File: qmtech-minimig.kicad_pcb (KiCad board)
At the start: 4 copper layers, 142.2 x 92 mm, 120 parts, among them IC1 RTL8211EG-VB-CG, J1 DB9_Male, J2 DB9_Male, J3 SCHA5B0200, J4 ARM_JTAG, J5 AUDIO-CONNECTOR-6P-SMD-344003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, J6 Mini-DIN-6, J7 HDMI_D_1.4, J8 HR911130A, SW1 SW_Push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

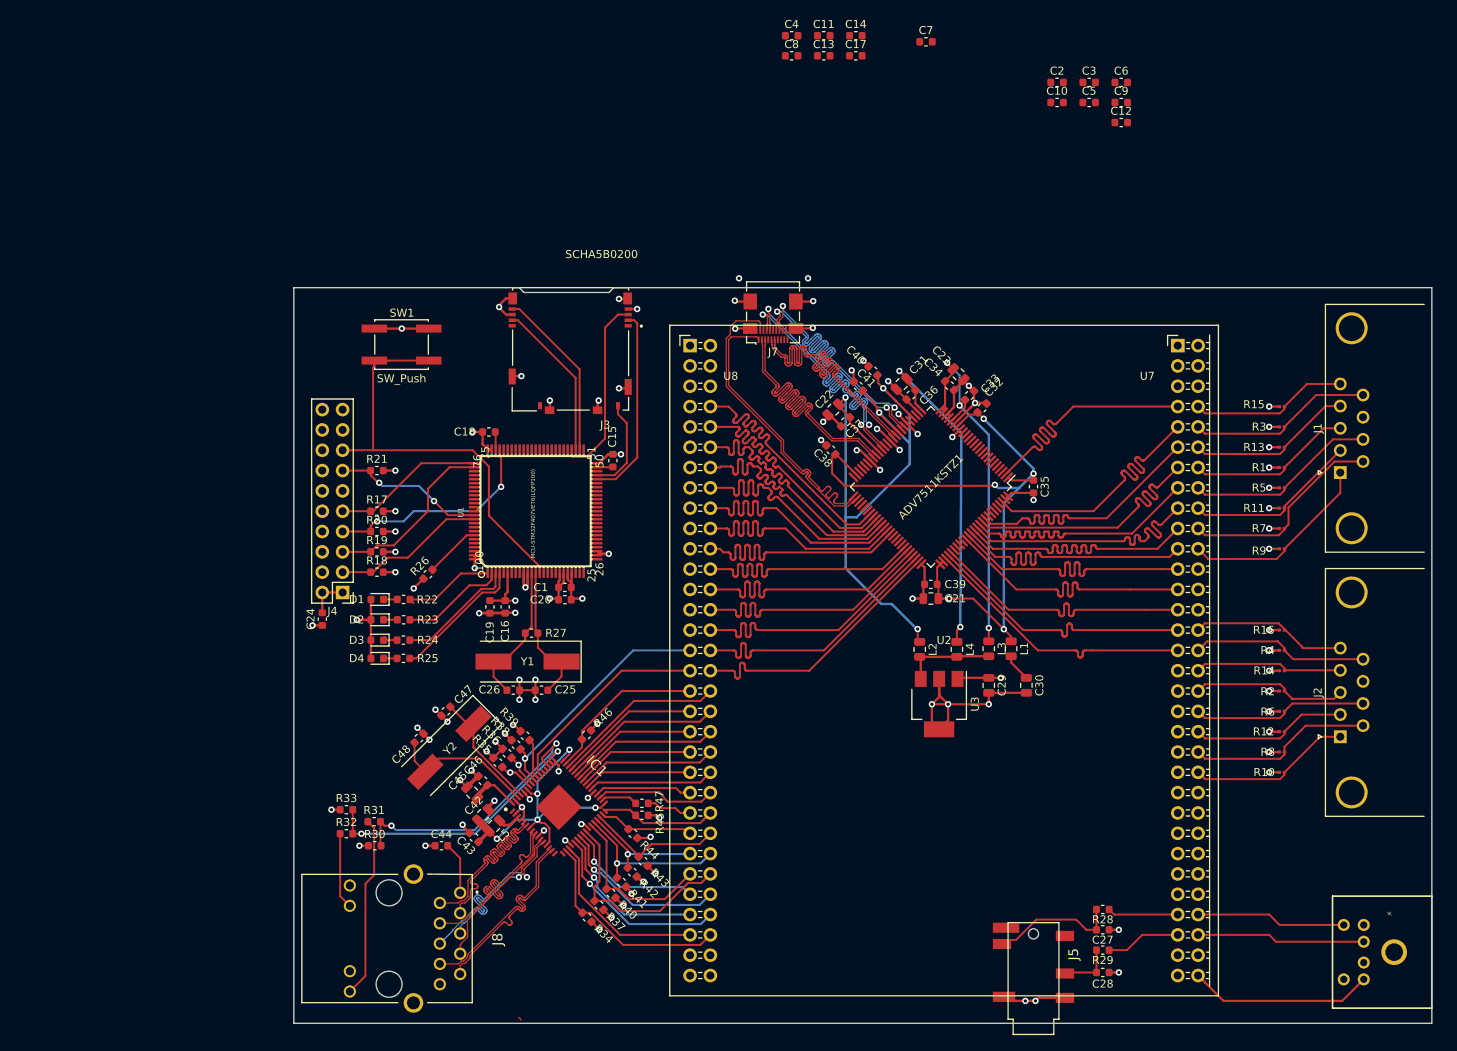
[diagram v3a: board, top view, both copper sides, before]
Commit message: Added protection diodes to the joystick ports.
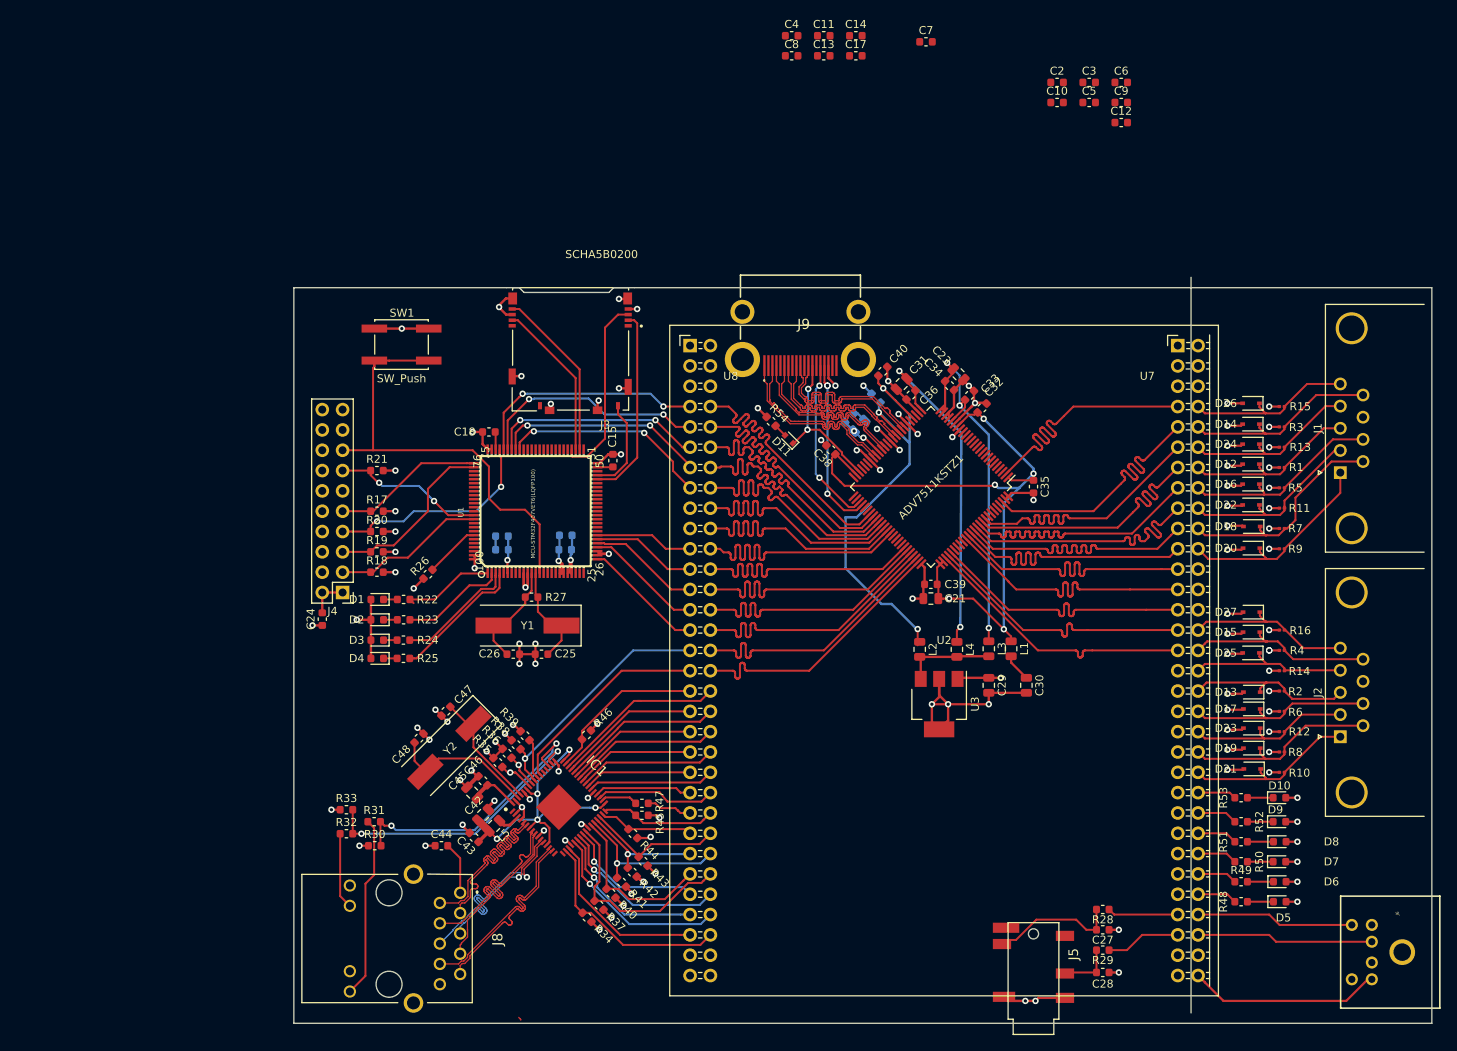
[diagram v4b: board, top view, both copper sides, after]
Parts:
- removed J7: HDMI_D_1.4, Connector_HDMI:HDMI_Micro-D_Molex_46765-0x01
- added D10: LED0, LED_SMD:LED_0603_1608Metric, F.Cu at (174.0, 127.0)
- added D11: D, Diode_SMD:D_SOD-523, F.Cu at (112.7, 82.2)
- added D12: D_Zener 3.6V BZT52C395, Diode_SMD:D_SOD-323, F.Cu at (170.4, 85.3)
- added D13: D_Zener 3.6V BZT52C395, Diode_SMD:D_SOD-323, F.Cu at (170.6, 113.8)
- added D14: D_Zener 3.6V BZT52C395, Diode_SMD:D_SOD-323, F.Cu at (170.4, 80.3)
- added D15: D_Zener 3.6V BZT52C395, Diode_SMD:D_SOD-323, F.Cu at (170.5, 106.3)
- added D16: D_Zener 3.6V BZT52C395, Diode_SMD:D_SOD-323, F.Cu at (170.4, 87.8)
- added D17: D_Zener 3.6V BZT52C395, Diode_SMD:D_SOD-323, F.Cu at (170.6, 115.9)
- added D18: D_Zener 3.6V BZT52C395, Diode_SMD:D_SOD-323, F.Cu at (170.6, 93.1)
- added D19: D_Zener 3.6V BZT52C395, Diode_SMD:D_SOD-323, F.Cu at (170.6, 120.8)
- added D20: D_Zener 3.6V BZT52C395, Diode_SMD:D_SOD-323, F.Cu at (170.5, 95.8)
- added D21: D_Zener 3.6V BZT52C395, Diode_SMD:D_SOD-323, F.Cu at (170.6, 123.4)
- added D22: D_Zener 3.6V BZT52C395, Diode_SMD:D_SOD-323, F.Cu at (170.4, 90.4)
- added D23: D_Zener 3.6V BZT52C395, Diode_SMD:D_SOD-323, F.Cu at (170.6, 118.3)
- added D24: D_Zener 3.6V BZT52C395, Diode_SMD:D_SOD-323, F.Cu at (170.4, 82.8)
- added D25: D_Zener 3.6V BZT52C395, Diode_SMD:D_SOD-323, F.Cu at (170.4, 108.9)
- added D26: D_Zener 3.6V BZT52C395, Diode_SMD:D_SOD-323, F.Cu at (170.4, 77.7)
- added D27: D_Zener 3.6V BZT52C395, Diode_SMD:D_SOD-323, F.Cu at (170.5, 103.8)
- added D5: LED5, LED_SMD:LED_0603_1608Metric, F.Cu at (174.0, 140.0)
- added D6: LED4, LED_SMD:LED_0603_1608Metric, F.Cu at (174.0, 137.5)
- added D7: LED3, LED_SMD:LED_0603_1608Metric, F.Cu at (174.0, 135.0)
- added D8: LED2, LED_SMD:LED_0603_1608Metric, F.Cu at (174.0, 132.5)
- added D9: LED1, LED_SMD:LED_0603_1608Metric, F.Cu at (174.0, 130.0)
- added J9: 47151-0001, 47151-0001-HDMI:47151-0001, F.Cu at (114.1, 61.7)
- added R48: 1k, Resistor_SMD:R_0603_1608Metric, F.Cu at (169.2, 140.0)
- added R49: 1k, Resistor_SMD:R_0603_1608Metric, F.Cu at (169.2, 137.5)
- added R50: 1k, Resistor_SMD:R_0603_1608Metric, F.Cu at (169.2, 135.0)
- added R51: 1k, Resistor_SMD:R_0603_1608Metric, F.Cu at (169.2, 132.5)
- added R52: 1k, Resistor_SMD:R_0603_1608Metric, F.Cu at (169.2, 130.0)
- added R53: 1k, Resistor_SMD:R_0603_1608Metric, F.Cu at (169.2, 127.0)
- added R54: 27K, Resistor_SMD:R_0603_1608Metric, F.Cu at (110.5, 80.0)
- C1, C16, C19, C20, C22, C37, C41: moved to B.Cu
- moved C16 8.86 mm to (76.8, 94.3), turned to 0 degrees
- moved C20 8.05 mm to (84.8, 94.2)
- moved C19 7.31 mm to (76.8, 96.0), turned to 180 degrees
- moved C1 4.71 mm to (84.7, 96.0)
- moved C25 4.50 mm to (81.8, 109.1)
- moved C26 4.50 mm to (78.2, 109.1)
- moved R27 4.50 mm to (80.5, 101.9)
- moved Y1 4.50 mm to (80.0, 105.5)
- moved C22 3.83 mm to (121.5, 80.5), turned to 45 degrees
- moved C41 2.67 mm to (123.6, 77.1)
- moved C40 1.23 mm to (124.4, 73.7), turned to 225 degrees
- moved J6 1.01 mm to (194.1, 146.3)
- moved C37 0.71 mm to (120.3, 79.5), turned to 45 degrees
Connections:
- net Net-(ADV7511KSTZ1-Pad12) renamed ADV_I2S0
- net Net-(ADV7511KSTZ1-Pad13) renamed ADV_I2S1
- net Net-(ADV7511KSTZ1-Pad14) renamed ADV_I2S2
- net Net-(ADV7511KSTZ1-Pad15) renamed ADV_I2S3
- net Net-(ADV7511KSTZ1-Pad16) renamed ADV_SCLK
- net Net-(ADV7511KSTZ1-Pad17) renamed ADV_LRCLK
- net Net-(ADV7511KSTZ1-Pad50) renamed ADV_CEC_CLK
- net Net-(ADV7511KSTZ1-Pad55) renamed ADV_SCL
- net Net-(ADV7511KSTZ1-Pad56) renamed ADV_SDA
- ADV7511KSTZ1 pad 48: Net-(ADV7511KSTZ1-Pad48) -> ADV_CEC
- ADV7511KSTZ1 pad 53: Net-(ADV7511KSTZ1-Pad53) -> ADV_DDCSCL
- ADV7511KSTZ1 pad 54: Net-(ADV7511KSTZ1-Pad54) -> ADV_DDCSDA
- U1 pad 26: Net-(U1-Pad26) -> STM_SPI1_CS
- U1 pad 29: Net-(U1-Pad29) -> STM_SPI1_NSS
- U1 pad 30: Net-(U1-Pad30) -> STM_SPI1_SCK
- U1 pad 31: Net-(U1-Pad31) -> STM_SPI1_MISO
- U1 pad 32: Net-(U1-Pad32) -> STM_SPI1_MOSI
- U1 pad 67: Net-(U1-Pad67) -> STM_USART1_CK
- U1 pad 68: Net-(U1-Pad68) -> STM_USART1_TX
- U1 pad 69: Net-(U1-Pad69) -> STM_USART1_RX
- U1 pad 70: Net-(U1-Pad70) -> STM_USART1_CTS
- U1 pad 71: Net-(U1-Pad71) -> STM_USART1_RTS
- U2 pad U711: Net-(U2-PadU711) -> STM_USART1_RX
- U2 pad U713: Net-(U2-PadU713) -> STM_USART1_TX
- U2 pad U715: Net-(U2-PadU715) -> STM_USART1_CK
- U2 pad U721: Net-(U2-PadU721) -> STM_SPI1_MOSI
- U2 pad U723: Net-(U2-PadU723) -> STM_SPI1_MISO
- U2 pad U725: Net-(U2-PadU725) -> STM_SPI1_SCK
- U2 pad U727: Net-(U2-PadU727) -> STM_SPI1_NSS
- U2 pad U729: Net-(U2-PadU729) -> STM_SPI1_CS
- U2 pad U77: Net-(U2-PadU77) -> STM_USART1_RTS
- U2 pad U79: Net-(U2-PadU79) -> STM_USART1_CTS
- U2 pad U846: Net-(U2-PadU846) -> /Main Board/LED0
- U2 pad U848: Net-(U2-PadU848) -> /Main Board/LED1
- U2 pad U850: Net-(U2-PadU850) -> /Main Board/LED2
- U2 pad U852: Net-(U2-PadU852) -> /Main Board/LED3
- U2 pad U854: Net-(U2-PadU854) -> /Main Board/LED4
- U2 pad U856: Net-(U2-PadU856) -> /Main Board/LED5
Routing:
- net ADV_HEAC+: track 37.4 -> 0.00 mm
- net ADV_HEAC-: track 37.3 -> 0.00 mm
- net STM_USART1_RTS: track 0.00 -> 29.5 mm, vias 0 -> 2
- net STM_USART1_CTS: track 0.00 -> 29.0 mm, vias 0 -> 2
- net STM_USART1_RX: track 0.00 -> 26.7 mm, vias 0 -> 2
- net STM_USART1_TX: track 0.00 -> 26.6 mm, vias 0 -> 2
- net STM_USART1_CK: track 0.00 -> 26.3 mm, vias 0 -> 2
- net ADV_DDCSDA: track 0.00 -> 21.6 mm, vias 0 -> 3
- net ADV_DDCSCL: track 0.00 -> 21.2 mm, vias 0 -> 2
- net ADV_AVDD: track 86.0 -> 65.3 mm, vias 4 -> 5
- net ADV_CEC: track 0.00 -> 19.5 mm, vias 0 -> 2
- net GND: track 184.6 -> 202.4 mm, vias 66 -> 75
- net STM_SPI1_CS: track 0.00 -> 15.2 mm
- net ADV_TX1-: track 38.0 -> 23.1 mm, vias 2 -> 0
- net ADV_TX2+: track 38.0 -> 23.1 mm
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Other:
- board size 142.2 x 92 mm -> 142.2 x 93.2 mm

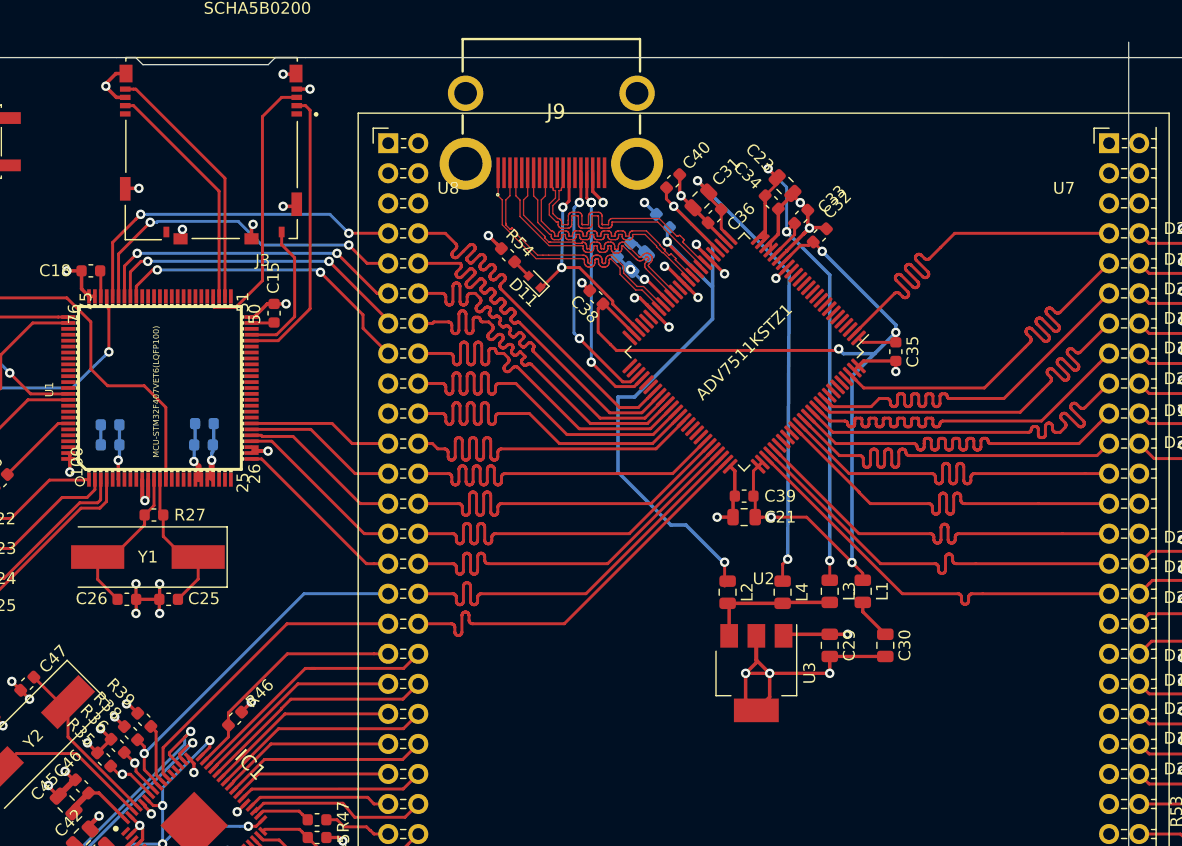
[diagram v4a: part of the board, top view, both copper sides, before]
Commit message: Added Control and audio lines to the ADV7511
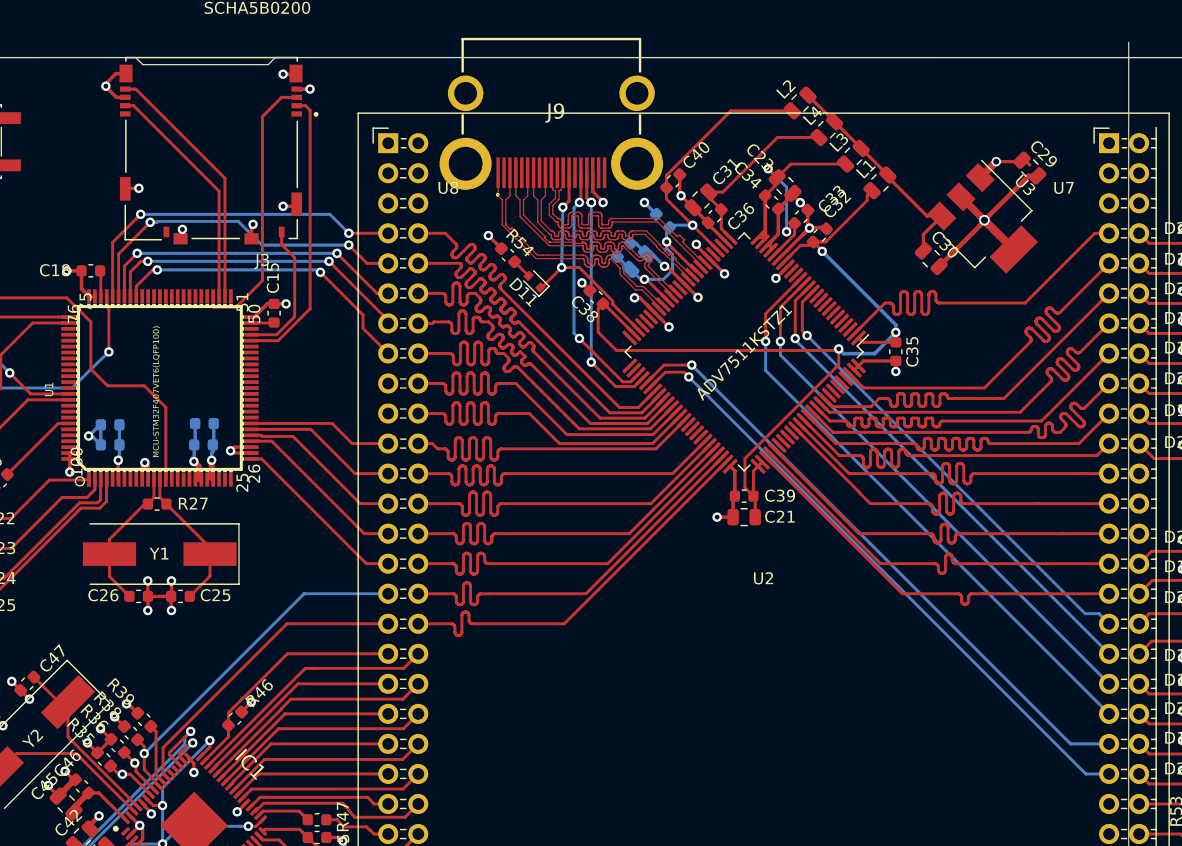
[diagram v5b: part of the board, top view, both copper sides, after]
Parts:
- moved C29 43.8 mm to (154.6, 72.6), turned to 315 degrees
- moved U3 42.8 mm to (151.0, 77.2), turned to 315 degrees
- moved L2 41.8 mm to (135.2, 67.1), turned to 45 degrees
- moved L4 39.3 mm to (137.4, 69.3), turned to 45 degrees
- moved L3 36.8 mm to (139.7, 71.6), turned to 45 degrees
- moved L1 34.6 mm to (141.9, 73.8), turned to 45 degrees
- moved C30 32.9 mm to (146.2, 80.2), turned to 315 degrees
- moved C25 1.03 mm to (82.8, 108.8)
- moved C26 1.03 mm to (79.2, 108.8)
- moved Y1 1.03 mm to (81.0, 105.2)
- moved R27 0.96 mm to (80.8, 101.0)
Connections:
- U2 pad U833: Net-(U2-PadU833) -> ADV_I2S0
- U2 pad U835: Net-(U2-PadU835) -> ADV_I2S1
- U2 pad U837: Net-(U2-PadU837) -> ADV_I2S2
- U2 pad U839: Net-(U2-PadU839) -> ADV_I2S3
- U2 pad U841: Net-(U2-PadU841) -> ADV_SCL
- U2 pad U843: Net-(U2-PadU843) -> ADV_SDA
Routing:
- net ADV_SDA: track 0.00 -> 53.3 mm, vias 0 -> 1
- net ADV_SCL: track 0.00 -> 53.0 mm, vias 0 -> 1
- net ADV_I2S3: track 0.00 -> 50.0 mm, vias 0 -> 1
- net ADV_I2S2: track 0.00 -> 46.2 mm, vias 0 -> 1
- net ADV_I2S1: track 0.00 -> 42.4 mm, vias 0 -> 1
- net ADV_I2S0: track 0.00 -> 39.8 mm, vias 0 -> 1
- net ADV_BGVDD: track 43.2 -> 15.8 mm, vias 2 -> 0
- net ADV_AVDD: track 65.3 -> 39.4 mm, vias 5 -> 3
- net ADV_PLVDD: track 52.2 -> 27.5 mm, vias 3 -> 2
- net ADV_DVDD: track 86.9 -> 79.7 mm, vias 5 -> 3
- net GND: track 202.4 -> 197.8 mm, vias 75 -> 74
- net /HDMI transmitter/1V8: track 15.0 -> 19.2 mm
- net Net-(C26-Pad2): track 13.5 -> 12.3 mm
- net Net-(C25-Pad2): track 14.1 -> 13.6 mm

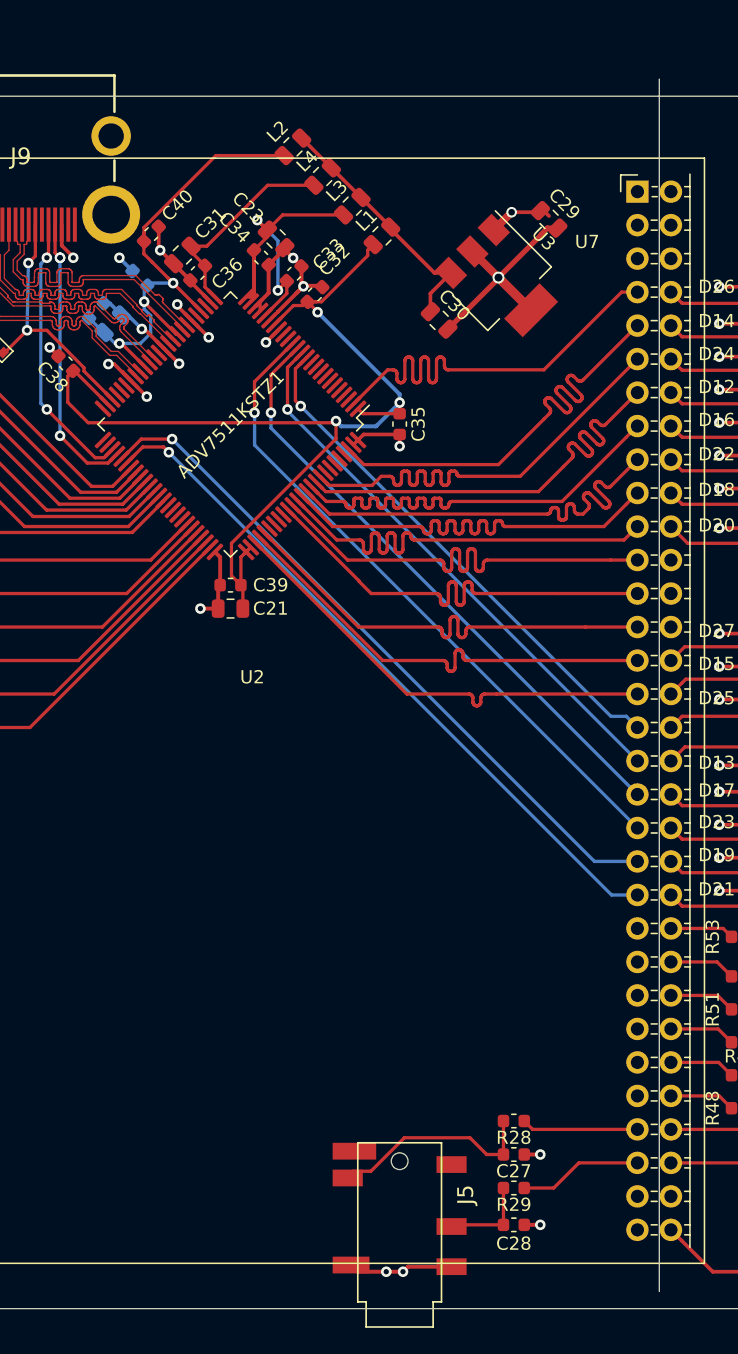
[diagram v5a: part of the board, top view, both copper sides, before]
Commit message: Removed edge that should not have been there.
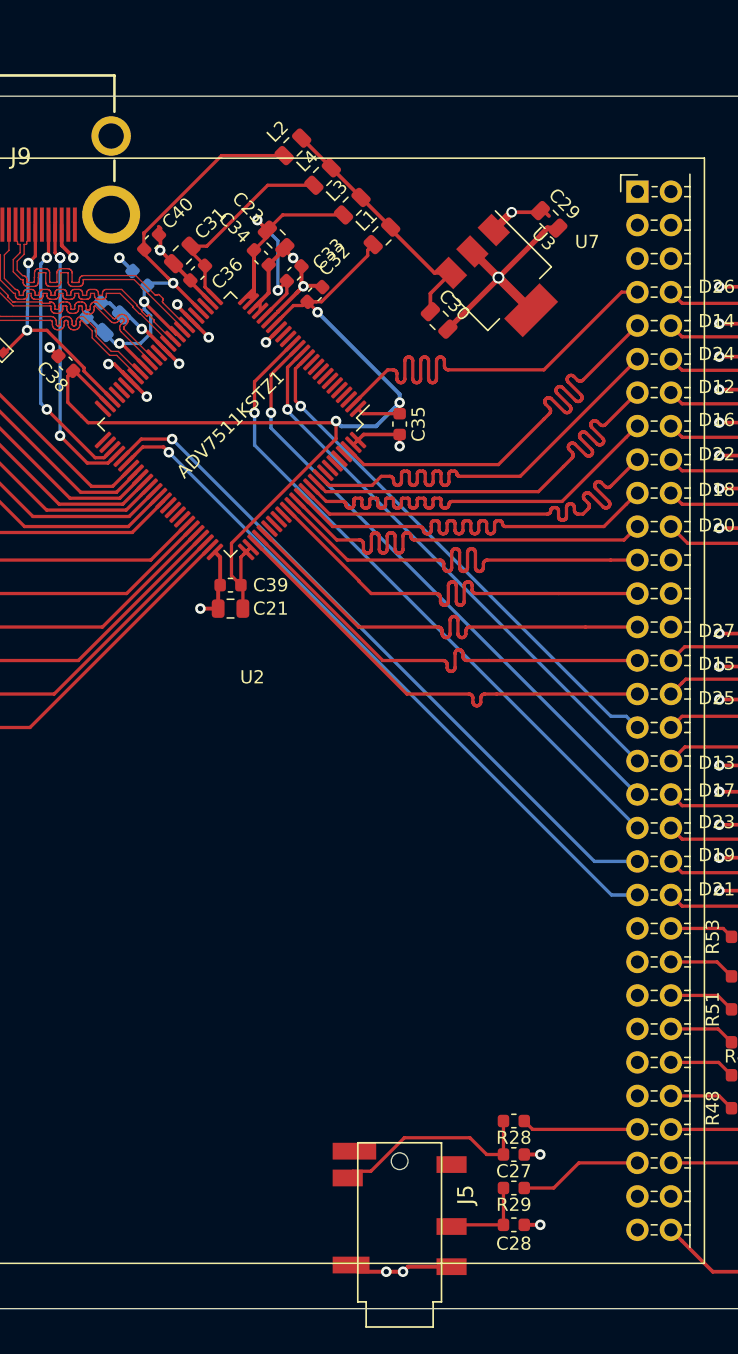
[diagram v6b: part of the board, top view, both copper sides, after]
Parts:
- moved C40 0.61 mm to (124.4, 74.3)
- moved C37 0.21 mm to (120.1, 79.4)
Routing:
- net (no net): track 1.39 -> 0.00 mm
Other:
- board size 142.2 x 93.2 mm -> 142.2 x 92 mm
